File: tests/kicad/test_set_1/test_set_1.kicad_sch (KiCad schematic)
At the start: 112 parts, among them J4 Conn_01x24_Socket

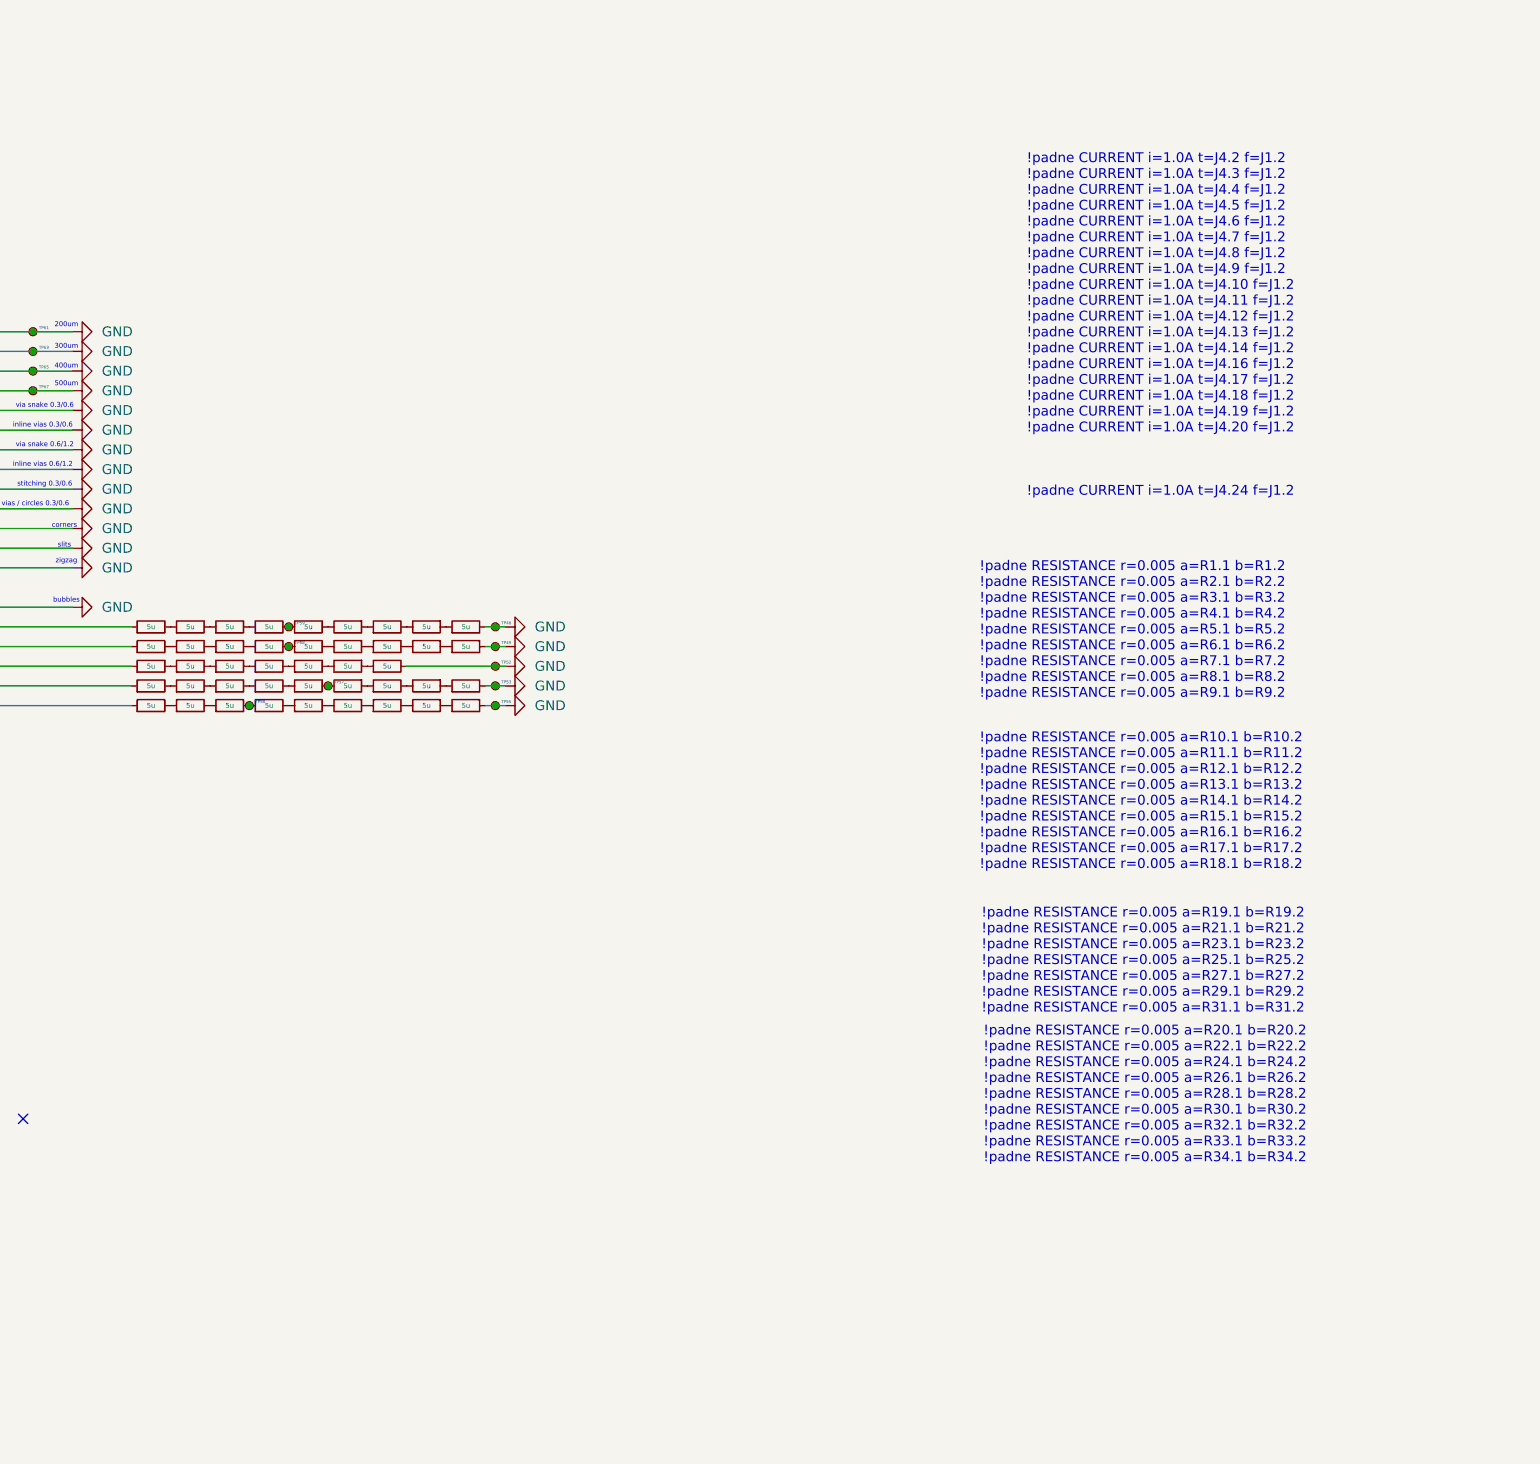
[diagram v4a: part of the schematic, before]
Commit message: test(test_set_1): Match sim parameters to real PCB
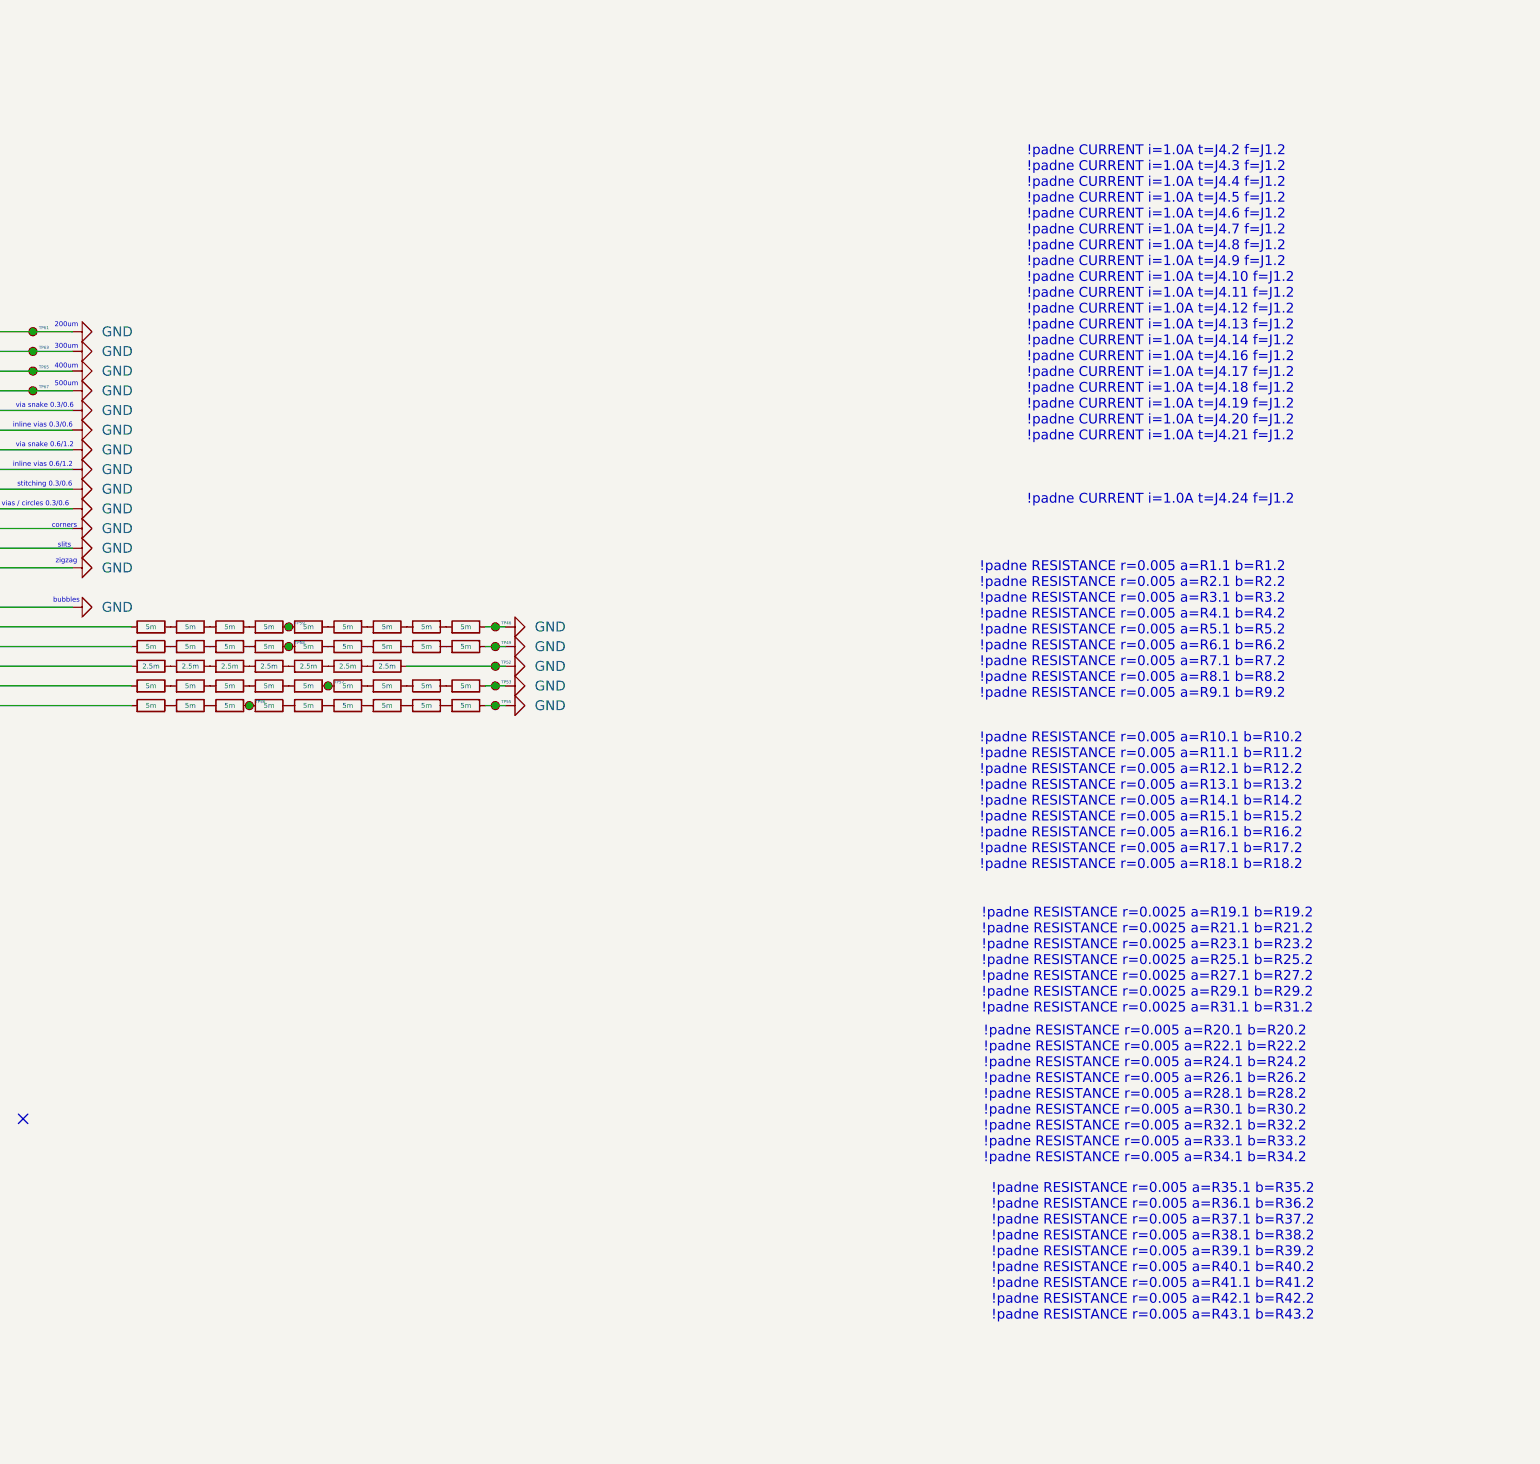
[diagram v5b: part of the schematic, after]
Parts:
- R1, R10, R11, R12, R13, R14, R15, R16, R17, R18, R2, R20, R22, R24, R26, R28, R3, R30, R32, R33, R34, R35, R36, R37, R38, R39, R4, R40, R41, R42, R43, R5, R6, R7, R8, R9: value 5u -> 5m
- R19, R21, R23, R25, R27, R29, R31: value 5u -> 2.5m
- TP1, TP10, TP11, TP12, TP13, TP14, TP15, TP16, TP17, TP18, TP19, TP2, TP20, TP21, TP22, TP23, TP24, TP25, TP26, TP27, TP28, TP29, TP3, TP30, TP31, TP32, TP33, TP34, TP35, TP36, TP37, TP38, TP39, TP4, TP40, TP41, TP42, TP43, TP44, TP45, TP46, TP47, TP48, TP49, TP5, TP50, TP51, TP52, TP53, TP54, TP55, TP56, TP57, TP58, TP59, TP6, TP60, TP61, TP62, TP63, TP64, TP65, TP66, TP67, TP7, TP8, TP9: value TestPoint_Small -> ~
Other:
- note added: "!padne RESISTANCE r=0.0025 a=R19.1 b=R19.2 !padne RESISTANCE r=0.0025 a=R21.1 b=R21.2 !padne RESISTANCE r=0.0025 a=R23.1 b=R23.2 !padne RESISTANCE r=0.0025 a=R25.1 b=R25.2 !padne RESISTANCE r=0.0025 a=R27.1 b=R27.2 !padne RESISTANCE r=0.0025 a=R29.1 b=R29.2 !padne RESISTANCE r=0.0025 a=R31.1 b=R31.2"
- note added: "!padne RESISTANCE r=0.005 a=R35.1 b=R35.2 !padne RESISTANCE r=0.005 a=R36.1 b=R36.2 !padne RESISTANCE r=0.005 a=R37.1 b=R37.2 !padne RESISTANCE r=0.005 a=R38.1 b=R38.2 !padne RESISTANCE r=0.005 a=R39.1 b=R39.2 !padne RESISTANCE r=0.005 a=R40.1 b=R40.2 !padne RESISTANCE r=0.005 a=R41.1 b=R41.2 !padne RESISTANCE r=0.005 a=R42.1 b=R42.2 !padne RESISTANCE r=0.005 a=R43.1 b=R43.2"
- note removed: "!padne RESISTANCE r=0.005 a=R19.1 b=R19.2 !padne RESISTANCE r=0.005 a=R21.1 b=R21.2 !padne RESISTANCE r=0.005 a=R23.1 b=R23.2 !padne RESISTANCE r=0.005 a=R25.1 b=R25.2 !padne RESISTANCE r=0.005 a=R27.1 b=R27.2 !padne RESISTANCE r=0.005 a=R29.1 b=R29.2 !padne RESISTANCE r=0.005 a=R31.1 b=R31.2"
